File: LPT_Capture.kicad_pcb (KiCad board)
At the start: 2 copper layers, 22 x 36 mm, 9 parts, among them J1 USB_B_Micro, J2 DB25 Male, U1 FT245RL

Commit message: layout fine tuning
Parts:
- C1: value 100nF -> 0.1uF
- moved C2 0.30 mm to (147.9, 97.5)
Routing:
- net /VBUS: track 20.1 -> 21.0 mm
- net GND: vias 3 -> 1

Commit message: tie select high
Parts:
- moved RN3 1.35 mm to (153.0, 89.7)
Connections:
- net /LD0 renamed /PD0
- net /LD1 renamed /PD1
- net /LD2 renamed /PD2
- net /LD3 renamed /PD3
- net /LD4 renamed /PD4
- net /LD5 renamed /PD5
- net /LD6 renamed /PD6
- net /LD7 renamed /PD7
- net Net-(J2-Pad15) renamed /RST_ERR
- C2 pad 1: /VBUS -> VCC
- J1 pad 1: /VBUS -> VCC
- J2 pad 1: Net-(J2-Pad1) -> /ACK
- J2 pad 10: Net-(J2-Pad1) -> /ACK
- J2 pad 11: Net-(J2-Pad11) -> /~BUSY
- J2 pad 13: (no net) -> /Select
- J2 pad 25: (no net) -> GND
- R1 pad 1: Net-(J2-Pad1) -> /ACK
- RN3 pad 1: /~TXE -> VCC
- RN3 pad 2: (no net) -> GND
- RN3 pad 3: /WR -> /~TXE
- RN3 pad 4: (no net) -> /WR
- RN3 pad 5: (no net) -> /ACK
- RN3 pad 6: Net-(J2-Pad1) -> /~BUSY
- RN3 pad 7: (no net) -> GND
- RN3 pad 8: Net-(J2-Pad11) -> /Select
- U1 pad 20: /VBUS -> VCC
- U1 pad 4: /VBUS -> VCC
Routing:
- net VCC: track 0.00 -> 33.5 mm, vias 0 -> 3
- net /ACK: track 0.00 -> 33.1 mm
- net Net-(J2-Pad1): track 33.1 -> 0.00 mm
- net /VBUS: track 21.0 -> 0.00 mm, vias 3 -> 0
- net /Select: track 0.00 -> 6.71 mm
- net /~BUSY: track 0.00 -> 4.58 mm
- net Net-(J2-Pad11): track 4.03 -> 0.00 mm
- net /~TXE: track 20.7 -> 19.3 mm
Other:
- board text added: "v002"

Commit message: small layout tweaks
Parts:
- moved RN3 2.11 mm to (153.0, 87.5)
- moved RN2 0.12 mm to (153.0, 98.6)
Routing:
- net /ACK: track 33.1 -> 36.1 mm
- net VCC: track 33.5 -> 35.6 mm
- net /WR: track 25.1 -> 27.2 mm
- net /~TXE: track 19.3 -> 21.2 mm
- net /Select: track 6.71 -> 4.88 mm

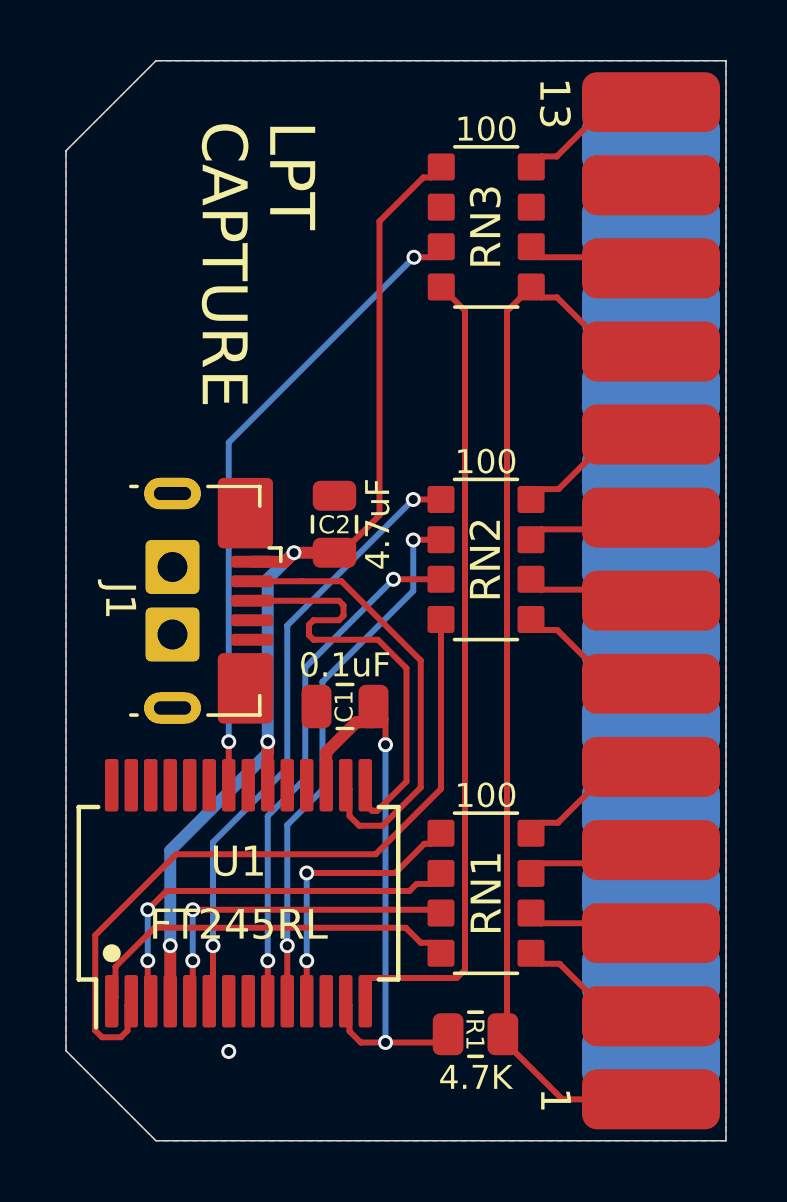
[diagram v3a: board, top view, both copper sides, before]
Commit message: inverted centered usb jack
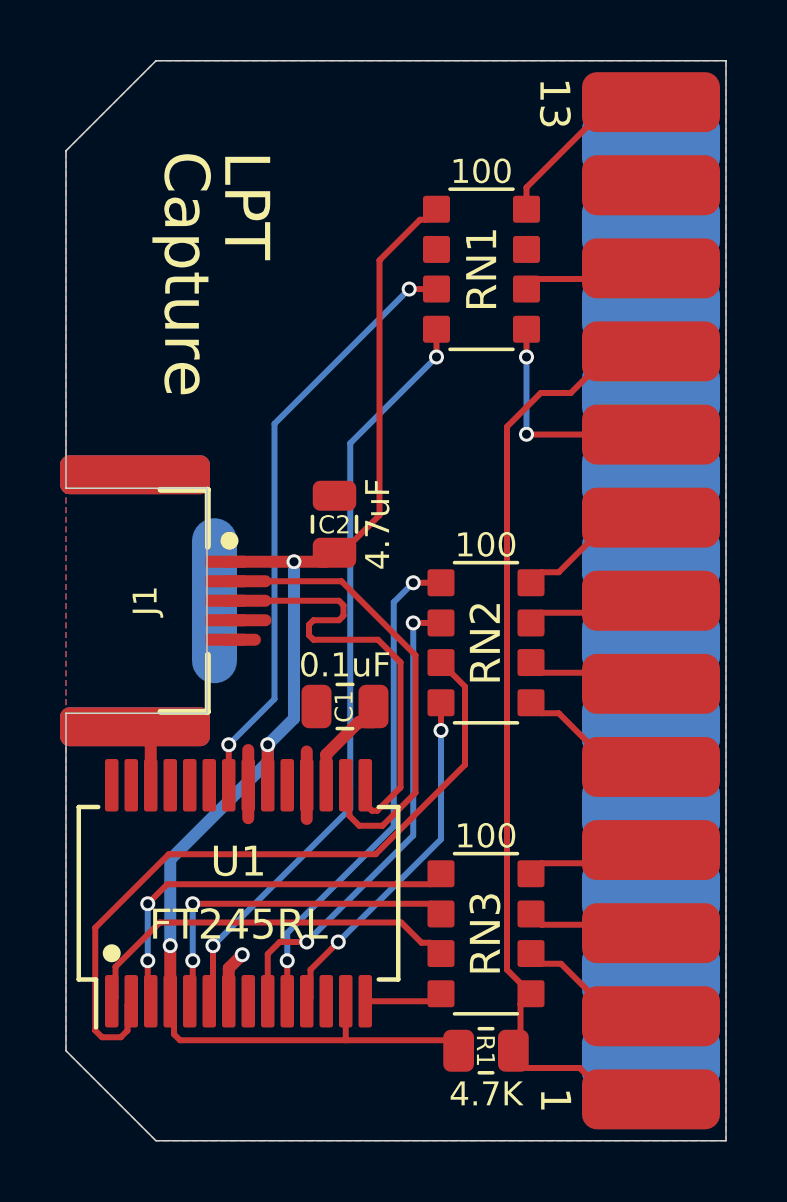
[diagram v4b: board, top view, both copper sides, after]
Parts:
- J1: footprint 000_LOCAL:USB_Micro-B_GCT_USB3076-30-A -> 000_LOCAL:GCT_USB3100-XX-X_inverted
- moved RN3 23.6 mm to (153.0, 111.1)
- moved RN1 20.8 mm to (152.8, 89.0)
- moved J1 2.80 mm to (140.9, 100.0)
- moved RN2 2.78 mm to (153.0, 101.4)
- moved R1 0.65 mm to (153.0, 115.0)
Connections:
- net /ACK renamed /~STROBE
- R1 pad 2: /3v3 -> VCC
- RN1 pad 1: /D3 -> VCC
- RN1 pad 2: /D2 -> GND
- RN1 pad 3: /D1 -> /~TXE
- RN1 pad 4: /D0 -> /D7
- RN1 pad 5: /PD0 -> /PD7
- RN1 pad 6: /PD1 -> /~BUSY
- RN1 pad 7: /PD2 -> GND
- RN1 pad 8: /PD3 -> /Select
- RN2 pad 1: /D7 -> /D6
- RN2 pad 2: /D6 -> /D5
- RN2 pad 3: /D5 -> /D4
- RN2 pad 4: /D4 -> /D3
- RN2 pad 5: /PD4 -> /PD3
- RN2 pad 6: /PD5 -> /PD4
- RN2 pad 7: /PD6 -> /PD5
- RN2 pad 8: /PD7 -> /PD6
- RN3 pad 1: VCC -> /D2
- RN3 pad 2: GND -> /D1
- RN3 pad 3: /~TXE -> /D0
- RN3 pad 6: /~BUSY -> /PD0
- RN3 pad 7: GND -> /PD1
- RN3 pad 8: /Select -> /PD2
- U1 pad 13: /3v3 -> VCC
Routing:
- net /WR: track 27.2 -> 2.63 mm
- net /3v3: track 19.6 -> 3.57 mm, vias 2 -> 0
- net GND: track 0.00 -> 12.5 mm
- net VCC: track 35.6 -> 46.7 mm
- net /D7: track 20.5 -> 25.5 mm
- net /~STROBE: track 36.1 -> 32.8 mm
- net /PD7: track 4.90 -> 7.65 mm, vias 0 -> 2
- net /D3: track 9.30 -> 11.8 mm
- net /D6: track 18.0 -> 16.6 mm
- net (no net): track 0.00 -> 1.33 mm
- net /D5: track 17.4 -> 16.1 mm
- net /~TXE: track 21.2 -> 19.9 mm
- net /Select: track 4.88 -> 6.05 mm
- net /PD6: track 4.30 -> 5.39 mm
- net /USB-: track 15.1 -> 15.8 mm
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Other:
- outline, holes or cut-outs redrawn
- board text added: "Capture"
- board text added: "v003"
- board text removed: "CAPTURE"
- board text removed: "v002"
